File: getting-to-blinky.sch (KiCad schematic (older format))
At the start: 9 parts, among them SW1 JS202011SCQN, U1 ICM7555

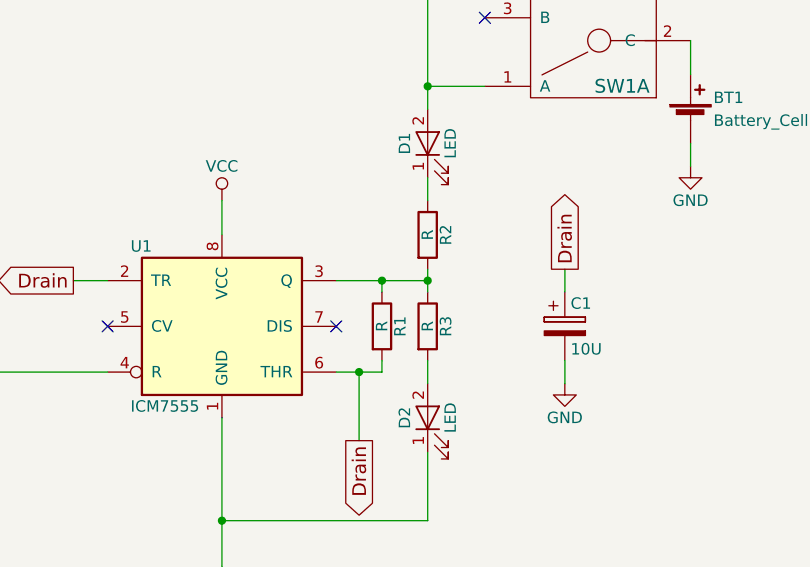
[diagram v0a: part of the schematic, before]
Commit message: Update values for components
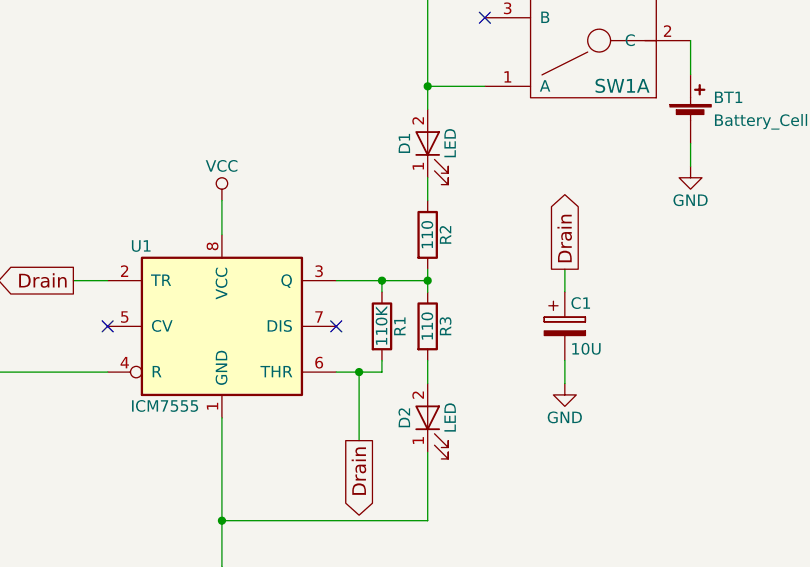
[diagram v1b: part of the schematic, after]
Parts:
- R1: value R -> 110K
- R2, R3: value R -> 110
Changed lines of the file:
@@
 P 5100 2700
 F 0 "R2" V 5180 2700 50  0000 C CNN
-F 1 "R" V 5100 2700 50  0000 C CNN
+F 1 "110" V 5100 2700 50  0000 C CNN
 F 2 "Resistors_SMD:R_0805_HandSoldering" V 5030 2700 50  0001 C CNN
 F 3 "" H 5100 2700 50  0001 C CNN
@@
 P 5100 3100
 F 0 "R3" V 5180 3100 50  0000 C CNN
-F 1 "R" V 5100 3100 50  0000 C CNN
+F 1 "110" V 5100 3100 50  0000 C CNN
 F 2 "Resistors_SMD:R_0805_HandSoldering" V 5030 3100 50  0001 C CNN
 F 3 "" H 5100 3100 50  0001 C CNN
@@
 P 4900 3100
 F 0 "R1" V 4980 3100 50  0000 C CNN
-F 1 "R" V 4900 3100 50  0000 C CNN
+F 1 "110K" V 4900 3100 50  0000 C CNN
 F 2 "Resistors_SMD:R_0805_HandSoldering" V 4830 3100 50  0001 C CNN
 F 3 "" H 4900 3100 50  0001 C CNN

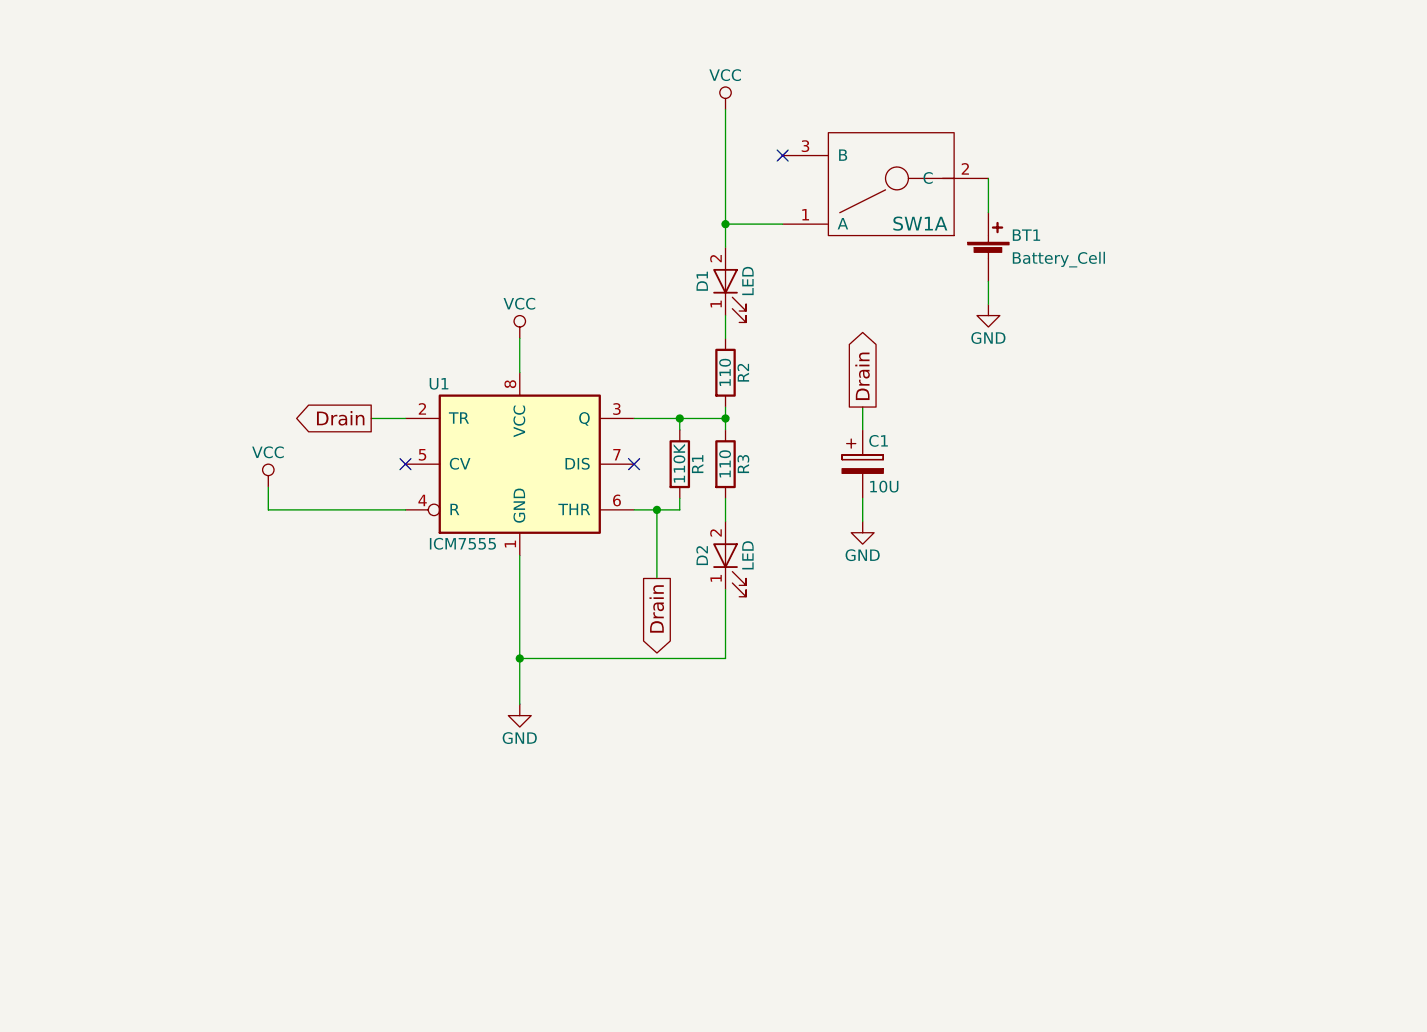
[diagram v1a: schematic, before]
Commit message: Re-worked blinky circuit with transistors due to limits of the 7555
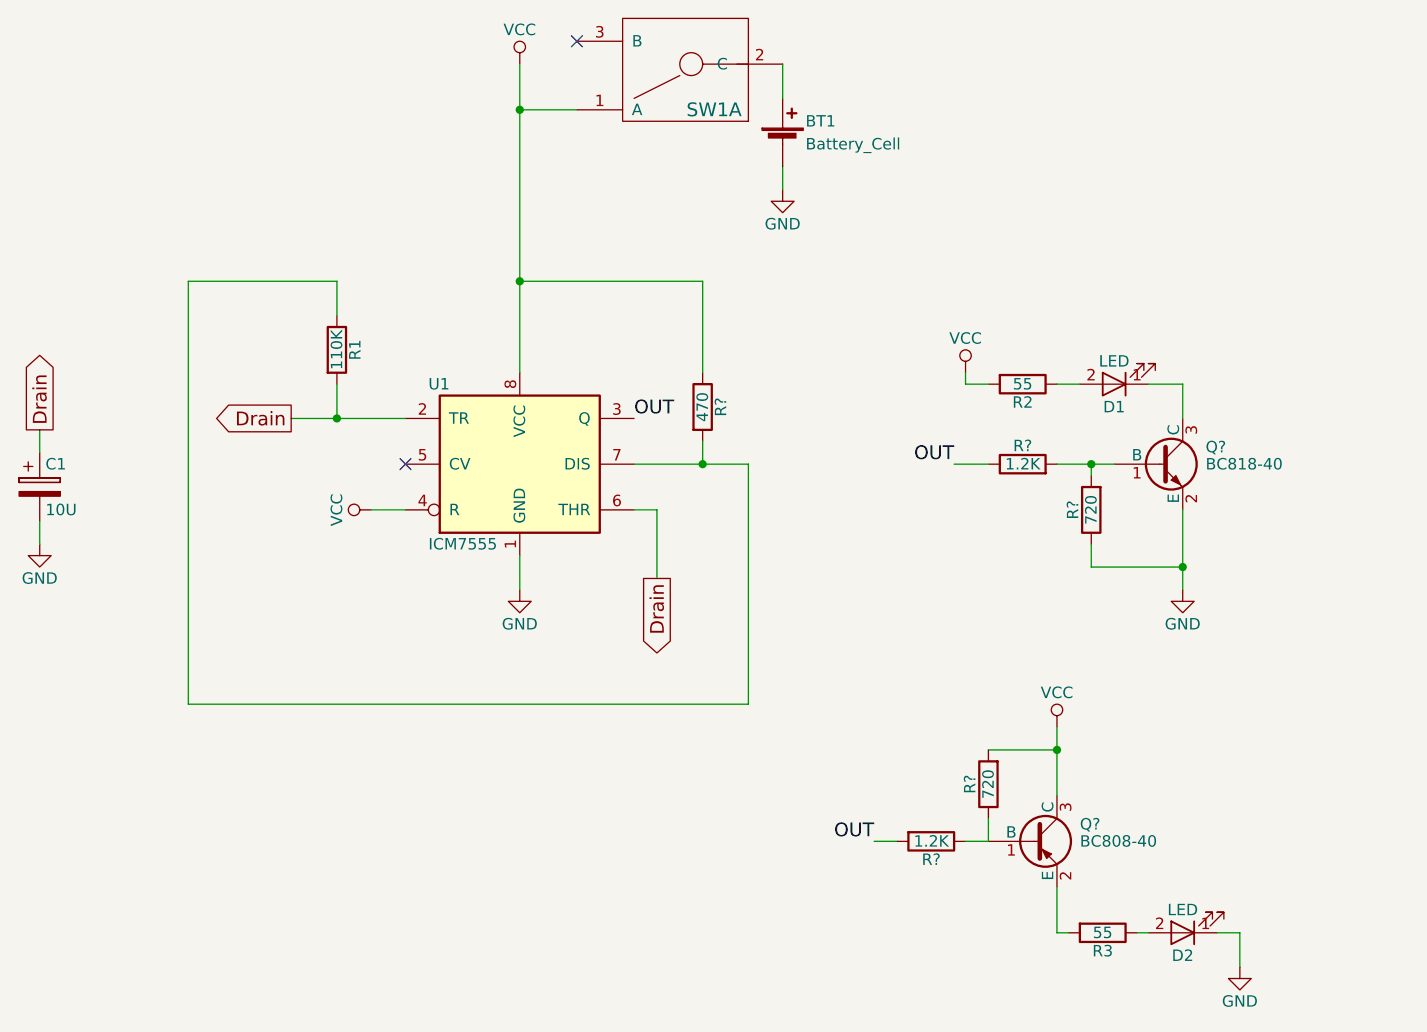
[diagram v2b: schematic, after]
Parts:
- added Q?: BC808-40, TO_SOT_Packages_SMD:SOT-23, symbol BC808-40
- added Q?: BC818-40, TO_SOT_Packages_SMD:SOT-23, symbol BC818-40
- added R?: 470, Resistors_SMD:R_0805_HandSoldering, symbol R
- added R? (x2): 1.2K, Resistors_SMD:R_0805_HandSoldering, symbol R
- added R? (x2): 720, Resistors_SMD:R_0805_HandSoldering, symbol R
- R2, R3: value 110 -> 55
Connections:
- net GND: now also Q?.2 (E), R?.1
- net VCC: now also R2.2, Q?.3 (C), R?.1, R?.2; no longer D1.2 (A)
- net at R2.1: now also D1.2 (A); no longer D1.1 (K)
- net at D2.2 (A): now also R3.1; no longer R3.2
- net at U1.7 (DIS): now also R1.1, R?.2
- new net: Q?.2 (E), R3.2
- new net: D1.1 (K), Q?.3 (C)
- new net: Q?.1 (B), R?.1, R?.1
- new net: Q?.1 (B), R?.2, R?.2
- new net OUT: R?.1, R?.2, U1.3 (Q)
- no-connect marks 3 -> 2
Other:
- moved on the sheet: BT1, C1, D1, D2, R1, R2, R3, SW1A

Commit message: Finalized and cleaned up the schematic and layed out Rev C
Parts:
- gave numbers to parts that had none: 7
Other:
- moved on the sheet: D1, D2, Q1, Q2, R2, R3, R5, R6, R7, R8

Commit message: Added parts for the new transistors
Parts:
- Q1: DKPN (none) -> BC80840MTFCT-ND; MPN (none) -> BC80840MTF
- Q2: DKPN (none) -> BC81840MTFCT-ND; MPN (none) -> BC81840MTF
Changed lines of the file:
@@
 F 1 "BC808-40" H 7100 3850 50  0000 L CNN
 F 2 "TO_SOT_Packages_SMD:SOT-23" H 7100 3775 50  0001 L CIN
-F 3 "" H 6900 3850 50  0001 L CNN
+F 3 "https://www.fairchildsemi.com/datasheets/BC/BC807.pdf" H 6900 3850 50  0001 L CNN
+F 4 "BC80840MTF" H 6900 3850 60  0001 C CNN "MPN"
+F 5 "BC80840MTFCT-ND" H 6900 3850 60  0001 C CNN "DKPN"
 	1    6900 3850
 	1    0    0    -1
@@
 F 1 "BC818-40" H 7650 2200 50  0000 L CNN
 F 2 "TO_SOT_Packages_SMD:SOT-23" H 7650 2125 50  0001 L CIN
-F 3 "" H 7450 2200 50  0001 L CNN
+F 3 "https://www.fairchildsemi.com/datasheets/BC/BC817.pdf" H 7450 2200 50  0001 L CNN
+F 4 "BC81840MTF" H 7450 2200 60  0001 C CNN "MPN"
+F 5 "BC81840MTFCT-ND" H 7450 2200 60  0001 C CNN "DKPN"
 	1    7450 2200
 	1    0    0    -1

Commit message: Fill in some missing information for the BOM
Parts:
- C1: DKPN (none) -> 478-8151-1-ND; MPN (none) -> F930J106MAA
- SW1: DKPN (none) -> 401-2002-1-ND; Digikey Part 401-2002-1-ND -> (none)
- U1: DKPN (none) -> ICM7555IBAZ-TCT-ND; MPN (none) -> ICM7555IBAZ-T
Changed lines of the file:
@@
 F 1 "10U" H 2125 3100 50  0000 L CNN
 F 2 "Capacitors_Tantalum_SMD:CP_Tantalum_Case-A_EIA-3216-18_Hand" H 2138 3050 50  0001 C CNN
-F 3 "" H 2100 3200 50  0001 C CNN
+F 3 "http://datasheets.avx.com/F93.pdf" H 2100 3200 50  0001 C CNN
+F 4 "F930J106MAA" H 2100 3200 60  0001 C CNN "MPN"
+F 5 "478-8151-1-ND" H 2100 3200 60  0001 C CNN "DKPN"
 	1    2100 3200
 	1    0    0    -1
@@
 F 1 "ICM7555" H 3800 2750 50  0000 L CNN
 F 2 "Housings_SOIC:SOIC-8_3.9x4.9mm_Pitch1.27mm" H 4200 3100 50  0001 C CNN
-F 3 "" H 4200 3100 50  0001 C CNN
+F 3 "http://www.intersil.com/content/dam/Intersil/documents/icm7/icm7555-56.pdf" H 4200 3100 50  0001 C CNN
+F 4 "ICM7555IBAZ-T" H 4200 3100 60  0001 C CNN "MPN"
+F 5 "ICM7555IBAZ-TCT-ND" H 4200 3100 60  0001 C CNN "DKPN"
 	1    4200 3100
 	1    0    0    -1
@@
 F 3 "http://www.ckswitches.com/media/1422/js.pdf" H 4850 750 60  0001 C CNN
 F 4 "JS202011SCQN" H 4950 850 60  0001 C CNN "MPN"
-F 5 "401-2002-1-ND" H 4950 950 60  0001 C CNN "Digikey Part"
+F 5 "401-2002-1-ND" H 4950 950 60  0001 C CNN "DKPN"
 F 6 "https://www.digikey.ca/product-detail/en/c-k/JS202011SCQN/401-2002-1-ND/1640098" H 4950 650 60  0001 C CNN "Digikey Singles Link"
 	1    4950 1350
